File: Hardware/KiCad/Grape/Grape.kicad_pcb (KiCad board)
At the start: 2 copper layers, 68.6 x 53.3 mm, 101 parts, among them J1 USB_MICROB, J19 POWER_JACKPTH, J3 ARDUINO_R3, P1 CONN_01X03, P10 CONN_01X03, P11 CONN_01X03, P12 CONN_01X03, P13 CONN_01X03, P14 CONN_01X03, P15 CONN_01X03, P16 CONN_01X03, P17 CONN_01X03, P18 CONN_01X03, P19 CONN_01X03, P2 CONN_01X03, P20 CONN_01X03, P21 CONN_01X03, P22 CONN_01X03, P23 I2C, P3 CONN_01X03, P4 CONN_01X03, P5 CONN_01X03, P6 CONN_01X03, P7 CONN_01X03, P8 CONN_01X03, P9 CONN_01X03, Q1 2N7002PW, Q4 FDN340P, Q5 FDN340P, SW1 SW_SPDT, U1 FT231XS, U2 LM358, U3 AMS1117-3.3, U4 ATMEGA328P_TQFP, U8 MP2307SO, Y1 16MHz

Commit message: Serigrafia web añadida
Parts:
- added G***: LOGO, Grape:nombre2, B.Cu at (141.1, 104.5)
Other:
- board text added: "0"
- board text added: "1"

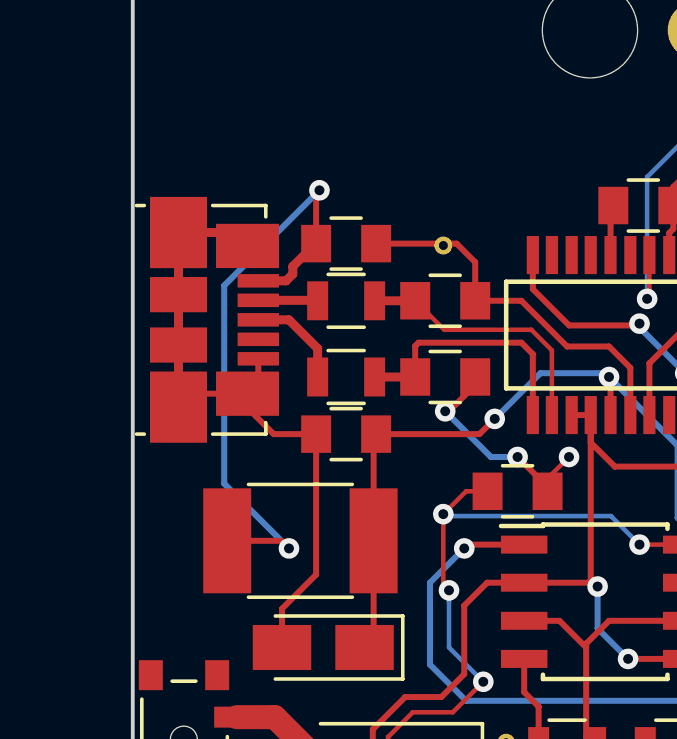
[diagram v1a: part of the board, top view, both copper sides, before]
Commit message: Usb cambiado
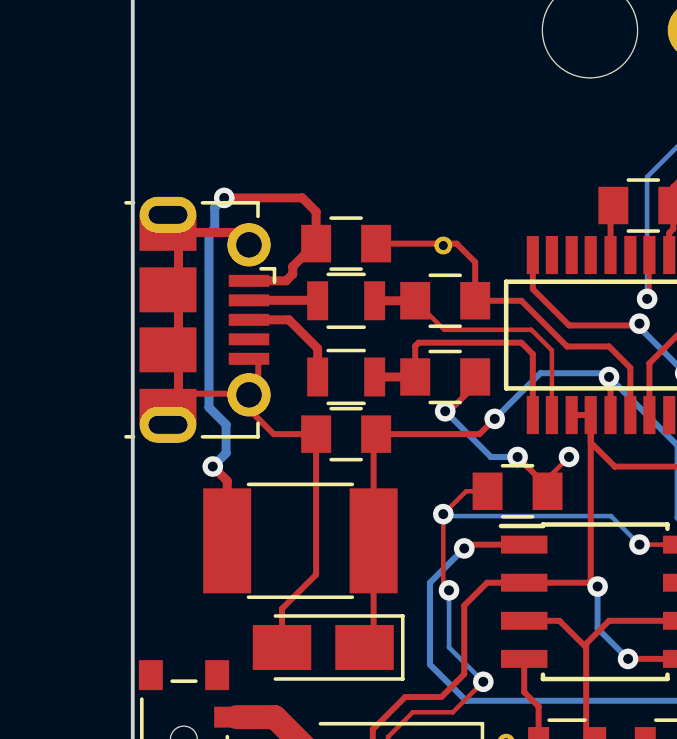
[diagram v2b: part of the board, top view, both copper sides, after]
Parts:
- J1: footprint Connectors_USB:USB_Micro-B_Molex_47346-0001 -> Connectors_USB:USB_Micro-B_Molex-105017-0001
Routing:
- net Net-(C4-Pad1): track 20.7 -> 19.2 mm

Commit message: Terminada
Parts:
- removed the G*** at (141.1, 104.5)
- added G***: LOGO, Grape:web2, B.Cu at (141.5, 104.1)
- added REF**: Fiducial_1mm_Dia_2mm_Outer, Fiducials:Fiducial_1mm_Dia_2mm_Outer, F.Cu at (123.2, 63.2)
- added REF**: Fiducial_1mm_Dia_2mm_Outer, Fiducials:Fiducial_1mm_Dia_2mm_Outer, F.Cu at (174.5, 106.7)
- added REF**: Fiducial_1mm_Dia_2mm_Outer, Fiducials:Fiducial_1mm_Dia_2mm_Outer, F.Cu at (118.4, 91.4)
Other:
- outline, holes or cut-outs redrawn
- board text added: "*Works as an Arduino Nano"
- board text added: "3V3"
- board text added: "5V"
- board text added: "AREF"
- board text added: "GND"
- board text added: "IOREF"
- board text added: "RESET"
- board text added: "SCL"
- board text added: "SDA"
- board text added: "VIN"
- board text added: "v2.0"
